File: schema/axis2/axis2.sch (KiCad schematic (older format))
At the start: 18 parts, among them J1 JA, J2 JB, J3 5VPower, J4 12VPower, J5 Power Motor 1, J6 Power Motor 2, J7 M1, J8 M2, J9 RC-PPM, Q1 BC547, U1 gy-9250, U2 L7805, U3 axis2-frame

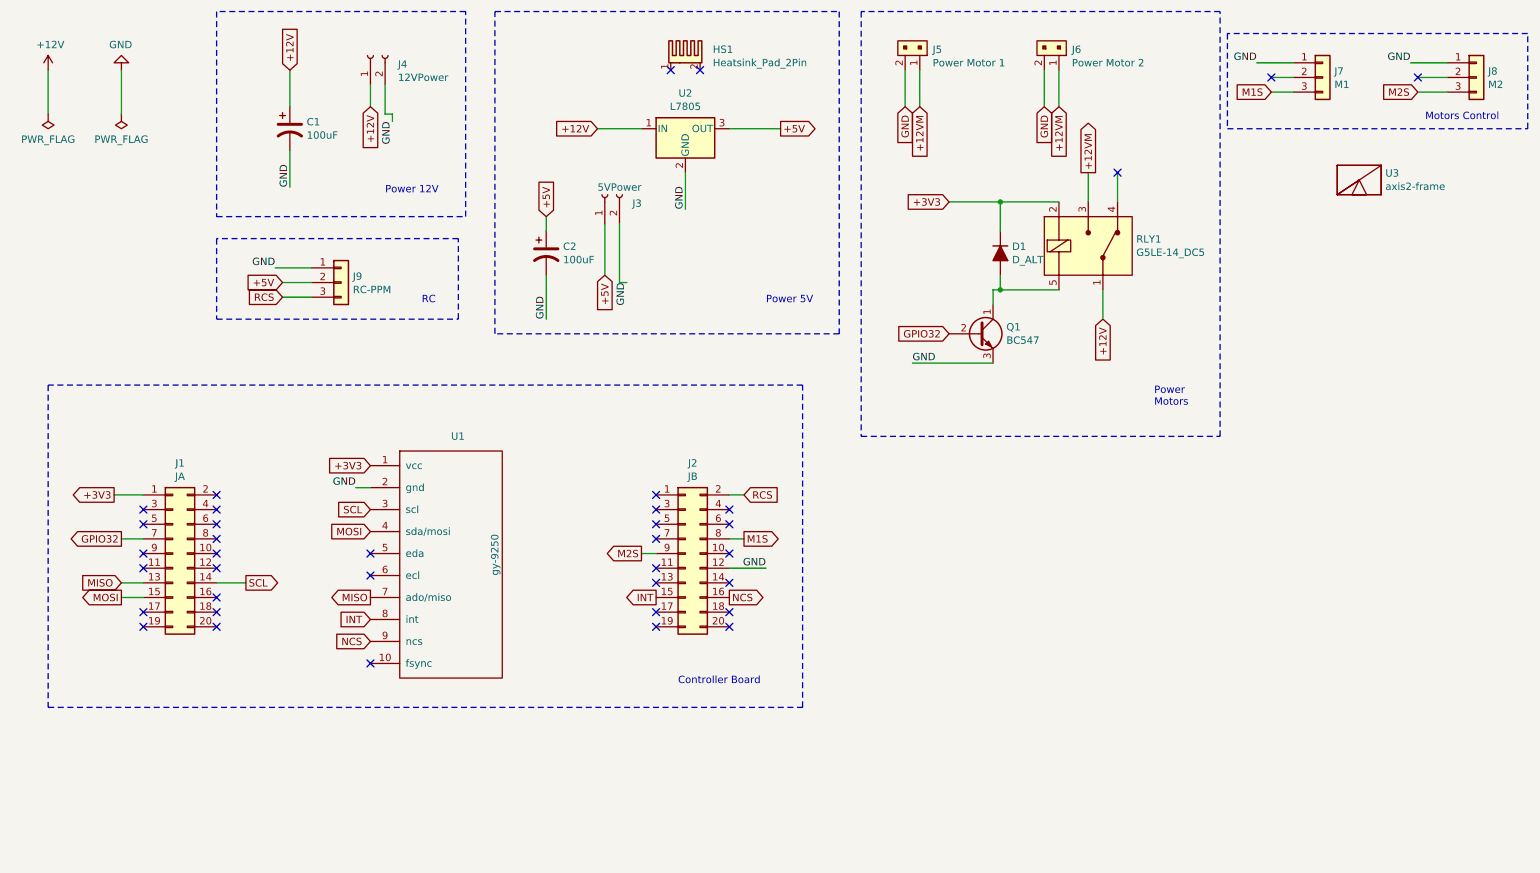
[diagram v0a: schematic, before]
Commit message: Corretto scheda. Erano invertiti i pin degli headers
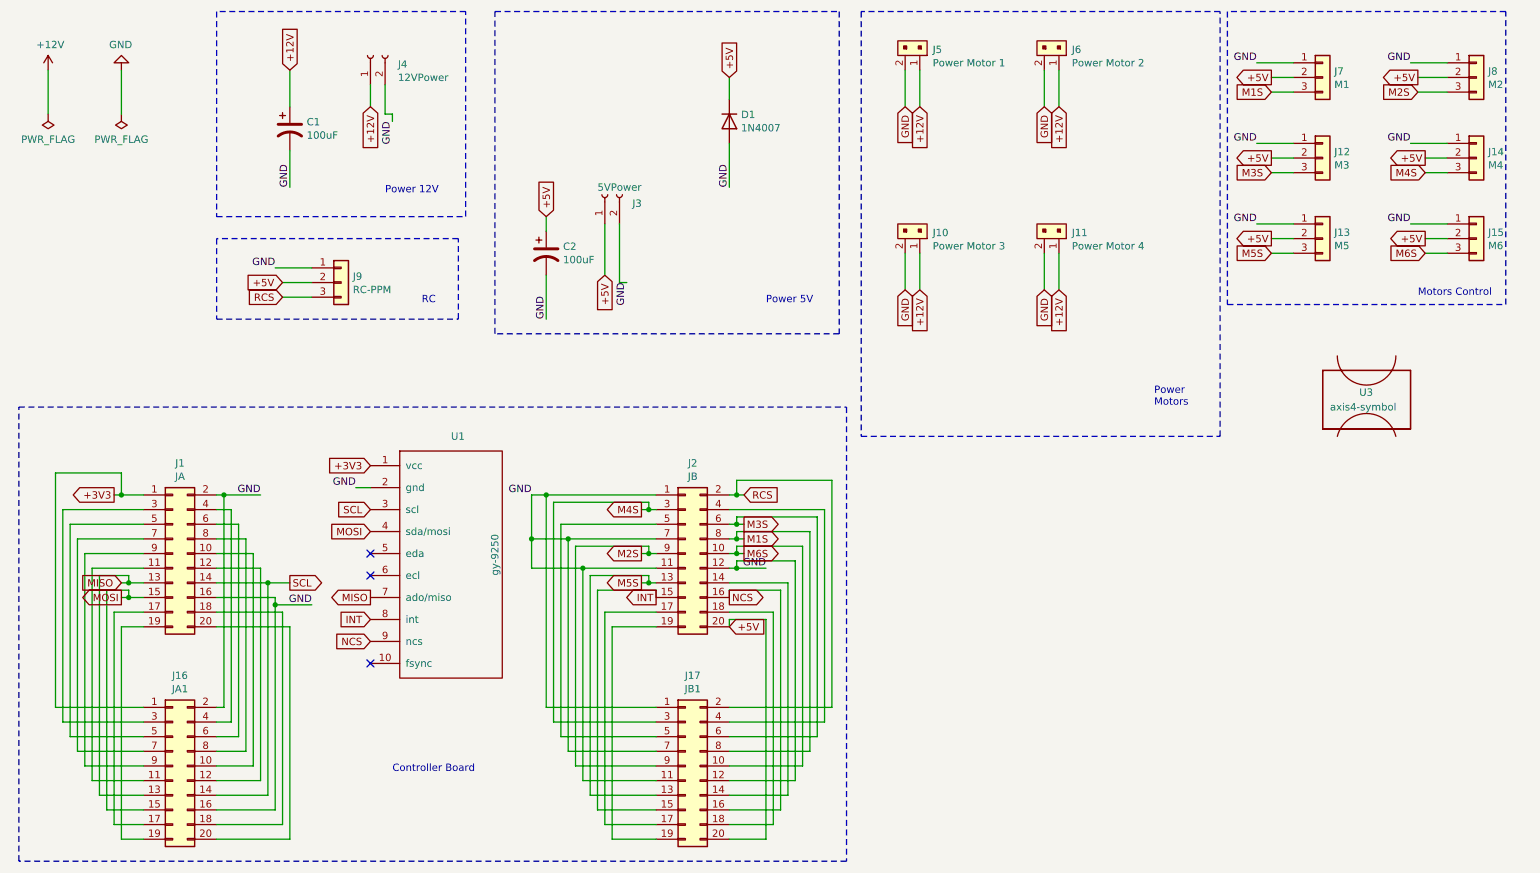
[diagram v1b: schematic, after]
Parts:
- removed D1: D_ALT, Diode_THT:D_DO-34_SOD68_P7.62mm_Horizontal, symbol Device:D_ALT
- removed HS1: Heatsink_Pad_2Pin, Heatsink:Heatsink_Stonecold_HS-132_32x14mm_2xFixation1.5mm, symbol axis2-rescue:Heatsink_Pad_2Pin-Mechanical
- removed Q1: BC547, Package_TO_SOT_THT:TO-92, symbol Transistor_BJT:BC547
- removed RLY1: G5LE-14_DC5, Relay_THT:Relay_SPDT_Omron-G5LE-1, symbol dk_Power-Relays-Over-2-Amps:G5LE-14_DC5
- removed U2: L7805, Package_TO_SOT_THT:TO-220-3_Vertical, symbol axis2-rescue:L7805-Regulator_Linear
- removed U3: axis2-frame, axis2:axis2-footprint, symbol axis2-symbols:axis2-frame
- added D1: 1N4007, Diode_THT:D_DO-41_SOD81_P10.16mm_Horizontal, symbol Diode:1N4007
- added J10: Power Motor 3, Connector:Deans, symbol dk_Rectangular-Connectors-Headers-Male-Pins:22-23-2021
- added J11: Power Motor 4, Connector:Deans, symbol dk_Rectangular-Connectors-Headers-Male-Pins:22-23-2021
- added J12: M3, Connector_PinHeader_2.54mm:PinHeader_1x03_P2.54mm_Horizontal, symbol Connector_Generic:Conn_01x03
- added J13: M5, Connector_PinHeader_2.54mm:PinHeader_1x03_P2.54mm_Horizontal, symbol Connector_Generic:Conn_01x03
- added J14: M4, Connector_PinHeader_2.54mm:PinHeader_1x03_P2.54mm_Horizontal, symbol Connector_Generic:Conn_01x03
- added J15: M6, Connector_PinHeader_2.54mm:PinHeader_1x03_P2.54mm_Horizontal, symbol Connector_Generic:Conn_01x03
- added J16: JA1, Connector_PinSocket_2.54mm:PinSocket_2x10_P2.54mm_Vertical, symbol axis2-rescue:Conn_02x10_Odd_Even-Connector_Generic
- added J17: JB1, Connector_PinSocket_2.54mm:PinSocket_2x10_P2.54mm_Vertical, symbol axis2-rescue:Conn_02x10_Odd_Even-Connector_Generic
- added U3: axis4-symbol, axis4:axis4-frame, symbol axis4:axis4-symbol
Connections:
- net +12VM is gone; now on net +12V: J5.1, J6.1
- net +12V: now also J10.1, J11.1
- net +3V3: now also J16.1 (Pin_1)
- net +5V: now also J2.20 (Pin_20), J7.2 (Pin_2), J8.2 (Pin_2), D1.1 (K), J12.2 (Pin_2), J13.2 (Pin_2), J14.2 (Pin_2), J15.2 (Pin_2), J17.20 (Pin_20)
- net GND: now also J1.16 (Pin_16), J1.2 (Pin_2), J2.1 (Pin_1), J2.11 (Pin_11), J2.7 (Pin_7), D1.2 (A), J10.2, J11.2, J12.1 (Pin_1), J13.1 (Pin_1), J14.1 (Pin_1), J15.1 (Pin_1), J16.16 (Pin_16), J16.2 (Pin_2), J17.1 (Pin_1), J17.11 (Pin_11), J17.12 (Pin_12), J17.7 (Pin_7)
- net INT: now also J17.15 (Pin_15)
- net M1S: now also J17.8 (Pin_8)
- net M2S: now also J17.9 (Pin_9)
- net MISO: now also J16.13 (Pin_13)
- net MOSI: now also J16.15 (Pin_15)
- net NCS: now also J17.16 (Pin_16)
- net RCS: now also J17.2 (Pin_2)
- net SCL: now also J16.14 (Pin_14)
- net at J1.10 (Pin_10): now also J16.10 (Pin_10)
- net at J1.11 (Pin_11): now also J16.11 (Pin_11)
- net at J1.12 (Pin_12): now also J16.12 (Pin_12)
- net at J1.17 (Pin_17): now also J16.17 (Pin_17)
- net at J1.18 (Pin_18): now also J16.18 (Pin_18)
- net at J1.19 (Pin_19): now also J16.19 (Pin_19)
- net at J1.20 (Pin_20): now also J16.20 (Pin_20)
- net at J1.3 (Pin_3): now also J16.3 (Pin_3)
- net at J1.4 (Pin_4): now also J16.4 (Pin_4)
- net at J1.5 (Pin_5): now also J16.5 (Pin_5)
- net at J1.6 (Pin_6): now also J16.6 (Pin_6)
- net at J1.8 (Pin_8): now also J16.8 (Pin_8)
- net at J1.9 (Pin_9): now also J16.9 (Pin_9)
- net M6S: now reaches J2.10 (Pin_10)
- net M6S: now also J15.3 (Pin_3), J17.10 (Pin_10)
- net M5S: now reaches J2.13 (Pin_13)
- net M5S: now also J13.3 (Pin_3), J17.13 (Pin_13)
- net at J2.14 (Pin_14): now also J17.14 (Pin_14)
- net at J2.17 (Pin_17): now also J17.17 (Pin_17)
- net at J2.18 (Pin_18): now also J17.18 (Pin_18)
- net at J2.19 (Pin_19): now also J17.19 (Pin_19)
- net M4S: now reaches J2.3 (Pin_3)
- net M4S: now also J14.3 (Pin_3), J17.3 (Pin_3)
- net at J2.4 (Pin_4): now also J17.4 (Pin_4)
- net at J2.5 (Pin_5): now also J17.5 (Pin_5)
- net M3S: now reaches J2.6 (Pin_6)
- net M3S: now also J12.3 (Pin_3), J17.6 (Pin_6)
- net GPIO32: no longer names the net of J1.7 (Pin_7)
- net GPIO32: now also J16.7 (Pin_7)
- no-connect marks 37 -> 3

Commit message: Tolto alimentazione 12V dalla scheda. Utilizzo alimentazione separata per i motori
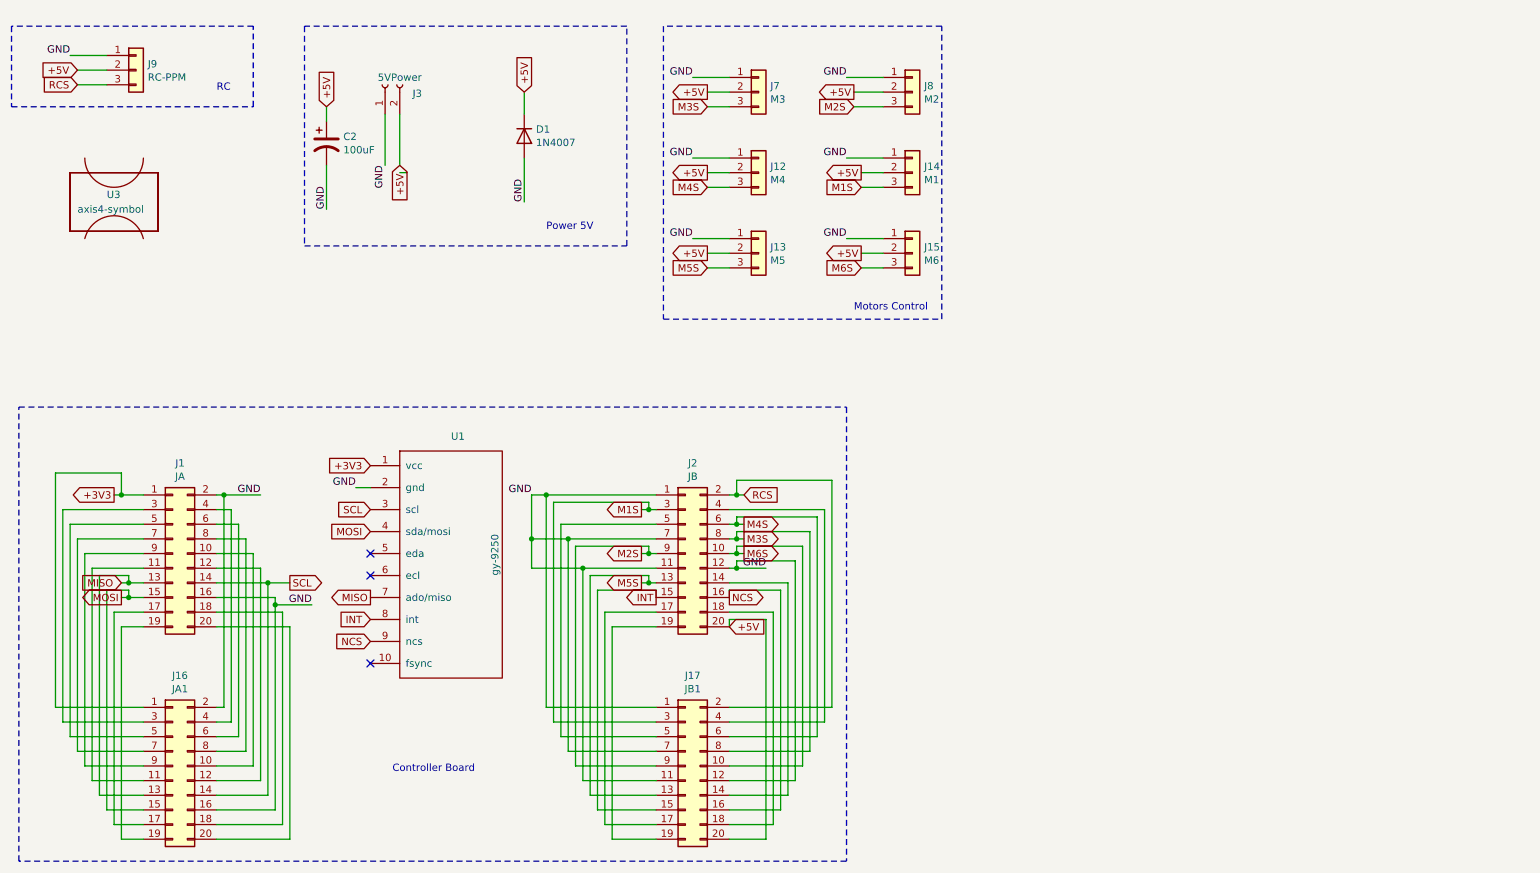
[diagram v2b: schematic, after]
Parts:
- removed C1: 100uF, Capacitor_THT:CP_Radial_D5.0mm_P2.50mm, symbol axis2-rescue:CP1-Device
- removed J10: Power Motor 3, Connector:Deans, symbol dk_Rectangular-Connectors-Headers-Male-Pins:22-23-2021
- removed J11: Power Motor 4, Connector:Deans, symbol dk_Rectangular-Connectors-Headers-Male-Pins:22-23-2021
- removed J4: 12VPower, Connector_BarrelJack:BarrelJack_Wuerth_6941xx301002, symbol axis2-rescue:Conn_01x02_Female-Connector
- removed J5: Power Motor 1, Connector:Deans, symbol dk_Rectangular-Connectors-Headers-Male-Pins:22-23-2021
- removed J6: Power Motor 2, Connector:Deans, symbol dk_Rectangular-Connectors-Headers-Male-Pins:22-23-2021
- J12: value M3 -> M4
- J14: value M4 -> M1
- J7: value M1 -> M3
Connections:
- net +5V: now also J3.2 (Pin_2); no longer J3.1 (Pin_1)
- net GND: now also J3.1 (Pin_1); no longer J3.2 (Pin_2)
- net M1S: now also J14.3 (Pin_3), J17.3 (Pin_3), J2.3 (Pin_3); no longer J17.8 (Pin_8), J2.8 (Pin_8), J7.3 (Pin_3)
- net M3S: now also J17.8 (Pin_8), J2.8 (Pin_8), J7.3 (Pin_3); no longer J12.3 (Pin_3), J17.6 (Pin_6), J2.6 (Pin_6)
- net M4S: now also J12.3 (Pin_3), J17.6 (Pin_6), J2.6 (Pin_6); no longer J14.3 (Pin_3), J17.3 (Pin_3), J2.3 (Pin_3)
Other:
- note removed: "Power 12V"
- note removed: "Power\nMotors"
- moved on the sheet: C2, D1, J12, J13, J14, J15, J3, J7, J8, J9, U3
